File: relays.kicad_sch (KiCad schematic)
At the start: 0 parts

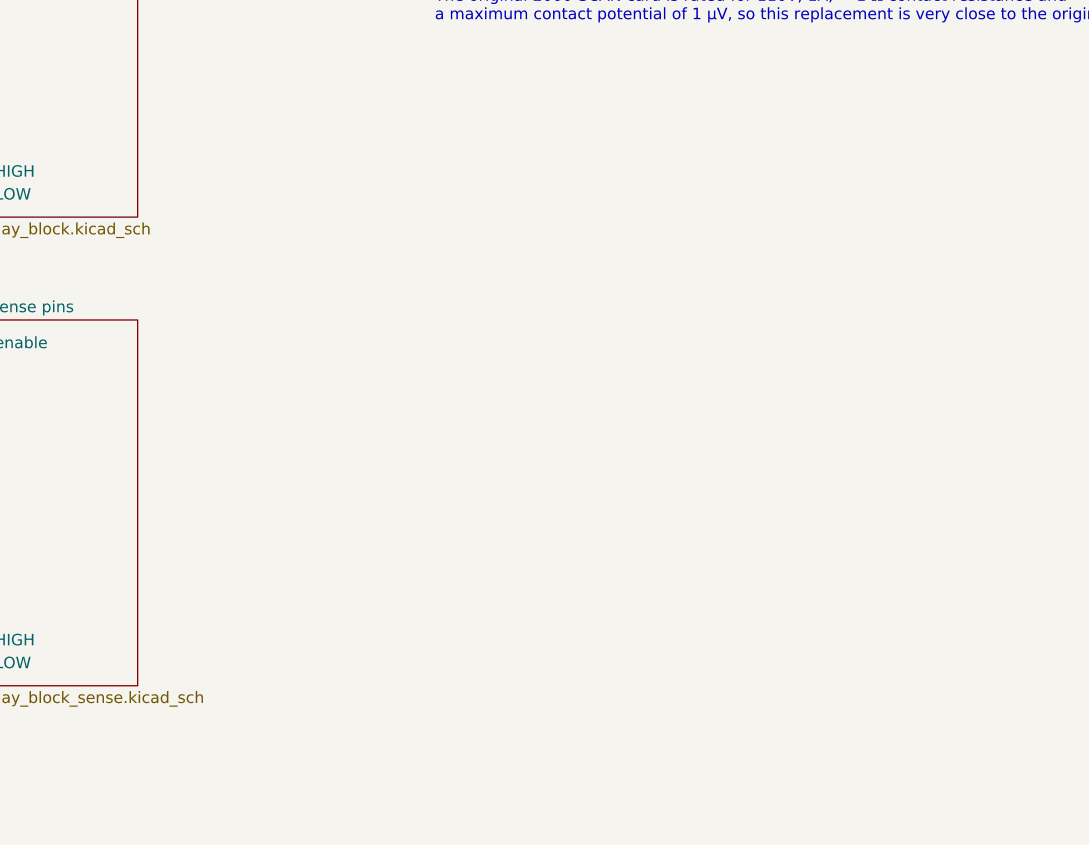
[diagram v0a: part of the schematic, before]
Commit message: added flatcable connector, updated doc
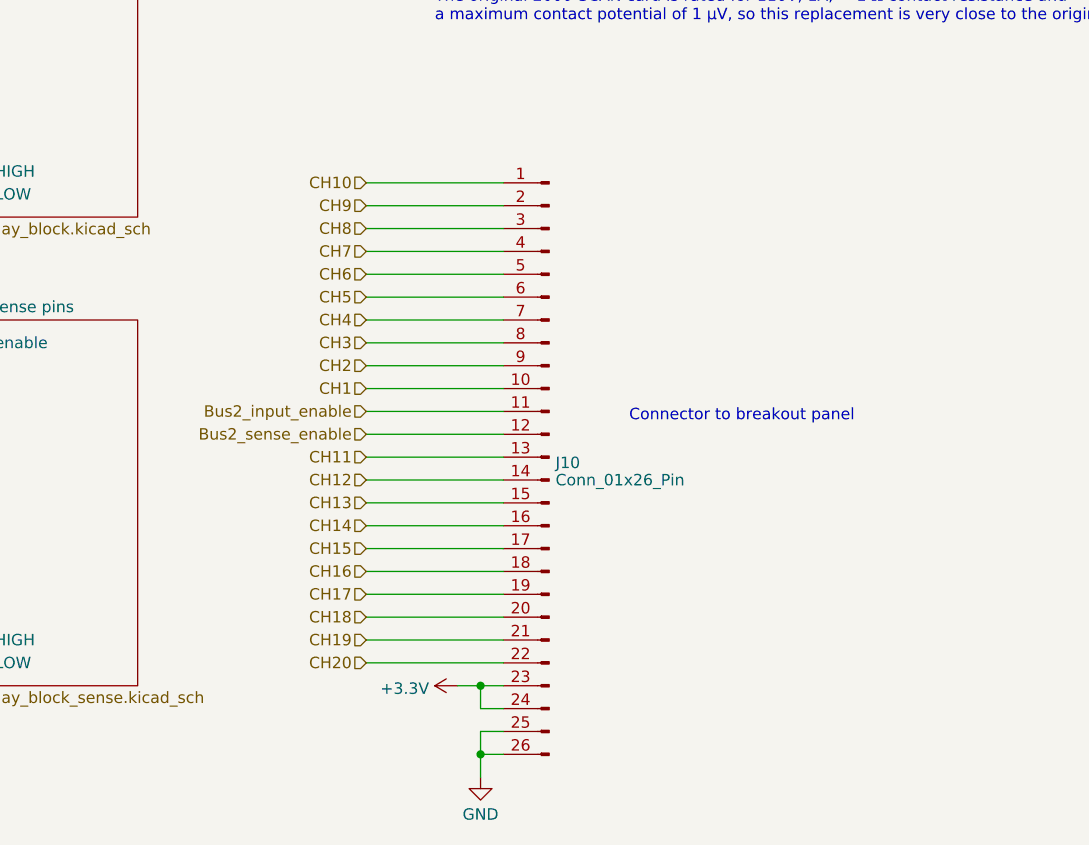
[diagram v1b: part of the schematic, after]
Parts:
- added J10: Conn_01x26_Pin, Connector_IDC:IDC-Header_2x13_P2.54mm_Latch_Horizontal, symbol Connector:Conn_01x26_Pin
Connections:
- net Bus2_input_enable: now also J10.11 (Pin_11)
- net Bus2_sense_enable: now also J10.12 (Pin_12)
- net CH1: now also J10.10 (Pin_10)
- net CH10: now also J10.1 (Pin_1)
- net CH11: now also J10.13 (Pin_13)
- net CH12: now also J10.14 (Pin_14)
- net CH13: now also J10.15 (Pin_15)
- net CH14: now also J10.16 (Pin_16)
- net CH15: now also J10.17 (Pin_17)
- net CH16: now also J10.18 (Pin_18)
- net CH17: now also J10.19 (Pin_19)
- net CH18: now also J10.20 (Pin_20)
- net CH19: now also J10.21 (Pin_21)
- net CH2: now also J10.9 (Pin_9)
- net CH20: now also J10.22 (Pin_22)
- net CH3: now also J10.8 (Pin_8)
- net CH4: now also J10.7 (Pin_7)
- net CH5: now also J10.6 (Pin_6)
- net CH6: now also J10.5 (Pin_5)
- net CH7: now also J10.4 (Pin_4)
- net CH8: now also J10.3 (Pin_3)
- net CH9: now also J10.2 (Pin_2)
- new net +3.3V: J10.23 (Pin_23), J10.24 (Pin_24)
- new net GND: J10.25 (Pin_25), J10.26 (Pin_26)
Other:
- note added: "Connector to breakout panel"

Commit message: update after component procurement problems
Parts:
- J10: MFN (none) -> Würth; PN (none) -> 61202622121
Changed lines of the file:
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@@
       (effects (font (size 1.27 1.27)) hide)
     )
-    (property "Datasheet" "~" (at 158.75 100.33 0)
+    (property "Datasheet" "https://www.we-online.com/components/products/datasheet/6120xx22121.pdf" (at 158.75 100.33 0)
       (effects (font (size 1.27 1.27)) hide)
     )
+    (property "MFN" "Würth" (at 158.75 100.33 0)
+      (effects (font (size 1.27 1.27)) hide)
+    )
+    (property "PN" "61202622121" (at 158.75 100.33 0)
+      (effects (font (size 1.27 1.27)) hide)
+    )

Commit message: better documentation
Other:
- note added: "STM32G070KBT6: max output sink/source IO current per pin = 15mA. max combined output sink/source IO current = 80mA. TLP3558A: Max trigger current = 3mA, but recommended current = 10mA. On 3.3V, with a 330R current limiter, the TLP3558A will draw 5.4mA max. Hence: About 11mA max per IO pin in the current config. Not a lot of headroom left. Therefore: If you want to connect a breakout panel, then e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"
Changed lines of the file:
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@@
+    (effects (font (size 1.27 1.27)) (justify left bottom))
+  )
+  (text "STM32G070KBT6: \nmax output sink/source IO current per pin = 15mA.\nmax combined output sink/source IO current = 80mA.\n\nTLP3558A: \nMax trigger current = 3mA, but recommended current = 10mA.\nOn 3.3V, with a 330R current limiter, the TLP3558A will draw 5.4mA max.\n\nHence: About 11mA max per IO pin in the current config. Not a lot of headroom left.\n\nTherefore: If you want to connect a breakout panel, then either:\n\n* do that on a 2000-SCAN board that is not equipped with optos\nor\n* use a breakout panel equipped with line drivers"
+    (at 167.64 142.24 0)
     (effects (font (size 1.27 1.27)) (justify left bottom))
   )
